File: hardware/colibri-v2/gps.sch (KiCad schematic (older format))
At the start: 11 parts

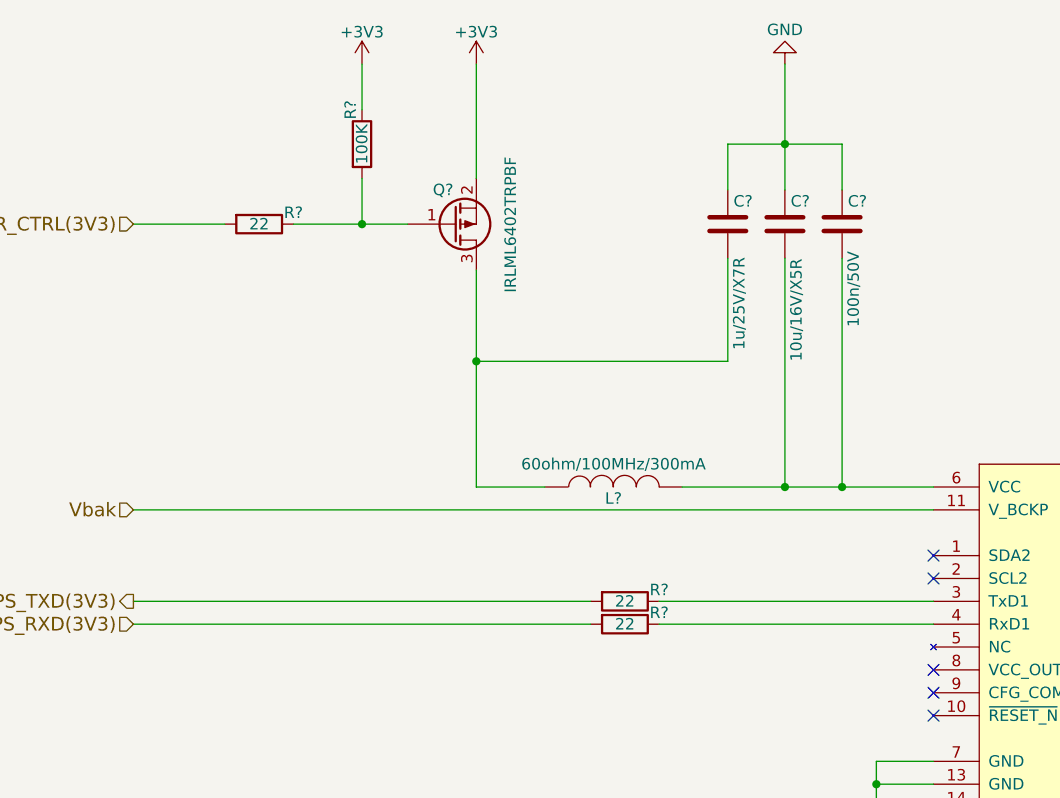
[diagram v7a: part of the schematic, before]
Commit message: Work on wandboard lcd and usb
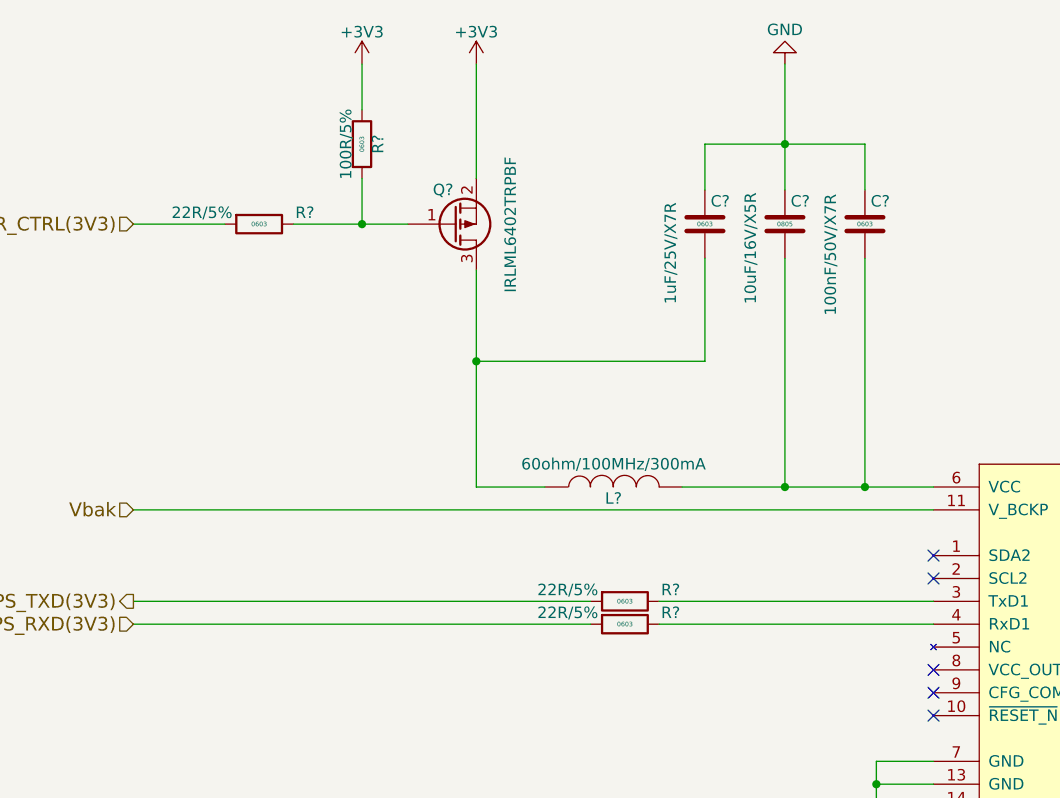
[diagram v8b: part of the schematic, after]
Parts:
- removed C?: 10u/16V/X5R, symbol C
- removed C?: 100n/50V, symbol C
- removed C?: 1u/25V/X7R, symbol C
- removed R? (x3): 22, Resistors_SMD:R_0603, symbol R
- removed R?: 100K, Resistors_SMD:R_0603, symbol R
- added C?: 100nF/50V/X7R, Capacitors_SMD:C_0603, symbol C_SMT
- added C?: 10uF/16V/X5R, Capacitors_SMD:C_0603, symbol C_SMT
- added C?: 1uF/25V/X7R, Capacitors_SMD:C_0603, symbol C_SMT
- added R?: 100R/5%, Resistors_SMD:R_0603, symbol R_SMT
- added R? (x3): 22R/5%, Resistors_SMD:R_0603, symbol R_SMT
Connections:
- net +3V3: now also R?.1
- net GND: now also C?.1, C?.1, C?.1
- net GPS_PWR_CTRL(3V3): now also R?.2
- net GPS_RXD(3V3): now also R?.2
- net GPS_TXD(3V3): now also R?.2
- net at U?.3 (TxD1): now also R?.1
- net at U?.4 (RxD1): now also R?.1
- net at L?.2, U?.6 (VCC): now also C?.2, C?.2
- net at Q?.1 (G): now also R?.1, R?.2
- net at L?.1, Q?.3 (D): now also C?.2
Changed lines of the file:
@@
 $EndDescr
-$Comp
-L R R?
-U 1 1 56139718
-P 4250 3650
-F 0 "R?" V 4200 3800 50  0000 C CNN
-F 1 "22" V 4250 3650 50  0000 C CNN
-F 2 "Resistors_SMD:R_0603" V 4180 3650 30  0001 C CNN
-F 3 "" H 4250 3650 30  0000 C CNN
-	1    4250 3650
-	0    1    1    0
-$EndComp
 $Comp
 L LEA-6S U?
@@
 	1    6400 3950
 	1    0    0    -1
-$EndComp
-$Comp
-L R R?
-U 1 1 561870DD
-P 4250 3750
-F 0 "R?" V 4200 3900 50  0000 C CNN
-F 1 "22" V 4250 3750 50  0000 C CNN
-F 2 "Resistors_SMD:R_0603" V 4180 3750 30  0001 C CNN
-F 3 "" H 4250 3750 30  0000 C CNN
-	1    4250 3750
-	0    1    1    0
 $EndComp
 Wire Wire Line
@@
 	3600 1300 3600 1800
 $Comp
-L C C?
-U 1 1 561882A0
-P 4950 2000
-F 0 "C?" H 4975 2100 50  0000 L CNN
-F 1 "10u/16V/X5R" V 5000 1400 50  0000 L CNN
-F 2 "" H 4988 1850 30  0001 C CNN
-F 3 "" H 4950 2000 60  0000 C CNN
-	1    4950 2000
-	1    0    0    -1
-$EndComp
-$Comp
-L C C?
-U 1 1 561883B9
-P 5200 2000
-F 0 "C?" H 5225 2100 50  0000 L CNN
-F 1 "100n/50V" V 5250 1550 50  0000 L CNN
-F 2 "" H 5238 1850 30  0001 C CNN
-F 3 "" H 5200 2000 60  0000 C CNN
-	1    5200 2000
-	1    0    0    -1
-$EndComp
-$Comp
-L C C?
-U 1 1 561884B4
-P 4700 2000
-F 0 "C?" H 4725 2100 50  0000 L CNN
-F 1 "1u/25V/X7R" V 4750 1450 50  0000 L CNN
-F 2 "" H 4738 1850 30  0001 C CNN
-F 3 "" H 4700 2000 60  0000 C CNN
-	1    4700 2000
-	1    0    0    -1
-$EndComp
-$Comp
 L GND #PWR?
 U 1 1 561885FB
@@
 $EndComp
 Wire Wire Line
-	4700 1850 4700 1650
-Wire Wire Line
-	4700 1650 5200 1650
-Wire Wire Line
-	5200 1650 5200 1850
+	4600 1850 4600 1650
+Wire Wire Line
+	4600 1650 5300 1650
 Wire Wire Line
 	4950 1300 4950 1850
 Connection ~ 4950 1650
 Wire Wire Line
-	5200 2150 5200 3150
-Connection ~ 5200 3150
-Wire Wire Line
 	4950 2150 4950 3150
 Connection ~ 4950 3150
 Wire Wire Line
-	4700 2150 4700 2600
-Wire Wire Line
-	4700 2600 3600 2600
+	4600 2150 4600 2600
+Wire Wire Line
+	4600 2600 3600 2600
 Connection ~ 3600 2600
 Text HLabel 2100 2000 0    60   Input ~ 0
 GPS_PWR_CTRL(3V3)
-$Comp
-L R R?
-U 1 1 5618877E
-P 2650 2000
-F 0 "R?" V 2600 2150 50  0000 C CNN
-F 1 "22" V 2650 2000 50  0000 C CNN
-F 2 "Resistors_SMD:R_0603" V 2580 2000 30  0001 C CNN
-F 3 "" H 2650 2000 30  0000 C CNN
-	1    2650 2000
-	0    1    1    0
-$EndComp
-$Comp
-L R R?
-U 1 1 561887E6
-P 3100 1650
-F 0 "R?" V 3050 1800 50  0000 C CNN
-F 1 "100K" V 3100 1650 50  0000 C CNN
-F 2 "Resistors_SMD:R_0603" V 3030 1650 30  0001 C CNN
-F 3 "" H 3100 1650 30  0000 C CNN
-	1    3100 1650
-	1    0    0    -1
-$EndComp
 $Comp
 L +3V3 #PWR?
@@
 Wire Wire Line
 	2100 3250 5600 3250
+$Comp
+L C_SMT C?
+U 1 1 56337F01
+P 5300 2000
+F 0 "C?" H 5325 2100 50  0000 L CNN
+F 1 "100nF/50V/X7R" V 5150 1600 50  0000 L CNN
+F 2 "Capacitors_SMD:C_0603" H 5330 1850 30  0001 L CNN
+F 3 "" H 5325 2100 60  0000 L CNN
+F 4 "0603" H 5300 2000 20  0000 C CNN "SMT"
+F 5 "1414028" H 5330 1810 30  0001 L CNN "Part"
+F 6 "Farnell" H 5330 1770 30  0001 L CNN "Provider"
+	1    5300 2000
+	1    0    0    -1
+$EndComp
+$Comp
+L C_SMT C?
+U 1 1 56338200
+P 4950 2000
+F 0 "C?" H 4975 2100 50  0000 L CNN
+F 1 "10uF/16V/X5R" V 4800 1650 50  0000 L CNN
+F 2 "Capacitors_SMD:C_0603" H 4980 1850 30  0001 L CNN
+F 3 "" H 4975 2100 60  0000 L CNN
+F 4 "0805" H 4950 2000 20  0000 C CNN "SMT"
+F 5 "1762635" H 4980 1810 30  0001 L CNN "Part"
+F 6 "Farnell" H 4980 1770 30  0001 L CNN "Provider"
+	1    4950 2000
+	1    0    0    -1
+$EndComp
+$Comp
+L C_SMT C?
+U 1 1 5633845A
+P 4600 2000
+F 0 "C?" H 4625 2100 50  0000 L CNN
+F 1 "1uF/25V/X7R" V 4450 1650 50  0000 L CNN
+F 2 "Capacitors_SMD:C_0603" H 4630 1850 30  0001 L CNN
+F 3 "" H 4625 2100 60  0000 L CNN
+F 4 "0603" H 4600 2000 20  0000 C CNN "SMT"
+F 5 "1735540" H 4630 1810 30  0001 L CNN "Part"
+F 6 "Farnell" H 4630 1770 30  0001 L CNN "Provider"
+	1    4600 2000
+	1    0    0    -1
+$EndComp
+Wire Wire Line
+	5300 1650 5300 1850
+Wire Wire Line
+	5300 2150 5300 3150
+Connection ~ 5300 3150
+$Comp
+L R_SMT R?
+U 1 1 5633999B
+P 3100 1650
+F 0 "R?" V 3170 1650 50  0000 C CNN
+F 1 "100R/5%" V 3030 1650 50  0000 C CNN
+F 2 "Resistors_SMD:R_0603" V 3250 1650 30  0001 C CNN
+F 3 "" V 3180 1650 30  0000 C CNN
+F 4 "0603" V 3100 1650 20  0000 C CNN "SMT"
+F 5 "9331689" V 3300 1650 30  0001 C CNN "Part"
+F 6 "Farnell" V 3350 1650 30  0001 C CNN "Provider"
+	1    3100 1650
+	1    0    0    -1
+$EndComp
+$Comp
+L R_SMT R?
+U 1 1 5633A992
+P 2650 2000
+F 0 "R?" V 2600 2200 50  0000 C CNN
+F 1 "22R/5%" V 2600 1750 50  0000 C CNN
+F 2 "Resistors_SMD:R_0603" V 2800 2000 30  0001 C CNN
+F 3 "" V 2730 2000 30  0000 C CNN
+F 4 "0603" V 2650 2000 20  0000 C CNN "SMT"
+F 5 "9331891" V 2850 2000 30  0001 C CNN "Part"
+F 6 "Farnell" V 2900 2000 30  0001 C CNN "Provider"
+	1    2650 2000
+	0    1    1    0
+$EndComp
+$Comp
+L R_SMT R?
+U 1 1 5633AA56
+P 4250 3650
+F 0 "R?" V 4200 3850 50  0000 C CNN
+F 1 "22R/5%" V 4200 3400 50  0000 C CNN
+F 2 "Resistors_SMD:R_0603" V 4400 3650 30  0001 C CNN
+F 3 "" V 4330 3650 30  0000 C CNN
+F 4 "0603" V 4250 3650 20  0000 C CNN "SMT"
+F 5 "9331891" V 4450 3650 30  0001 C CNN "Part"
+F 6 "Farnell" V 4500 3650 30  0001 C CNN "Provider"
+	1    4250 3650
+	0    1    1    0
+$EndComp
+$Comp
+L R_SMT R?
+U 1 1 5633AB3E
+P 4250 3750
+F 0 "R?" V 4200 3950 50  0000 C CNN
+F 1 "22R/5%" V 4200 3500 50  0000 C CNN
+F 2 "Resistors_SMD:R_0603" V 4400 3750 30  0001 C CNN
+F 3 "" V 4330 3750 30  0000 C CNN
+F 4 "0603" V 4250 3750 20  0000 C CNN "SMT"
+F 5 "9331891" V 4450 3750 30  0001 C CNN "Part"
+F 6 "Farnell" V 4500 3750 30  0001 C CNN "Provider"
+	1    4250 3750
+	0    1    1    0
+$EndComp
 $EndSCHEMATC
